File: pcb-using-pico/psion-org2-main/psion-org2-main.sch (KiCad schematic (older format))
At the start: 83 parts, among them J1 Conn_01x24_Female, J2 Conn_01x03_Female, J3 Conn_01x27_Female, J4 Conn_01x02_Female, J5 Conn_01x02_Female, J6 Conn_01x11_Female, M1 P-CHANNEL-MOSFET, M2 P-CHANNEL-MOSFET, M3 P-CHANNEL-MOSFET, U1 Pico, U10 AMS1117-3.3, U2 74HC595, U3 Regulator_Switching_MT3608, U4 74LS165, U5 74HC595, U6 AMS1117-5.0, U7 MCP7940N-xSN, Y1 32k768Hz

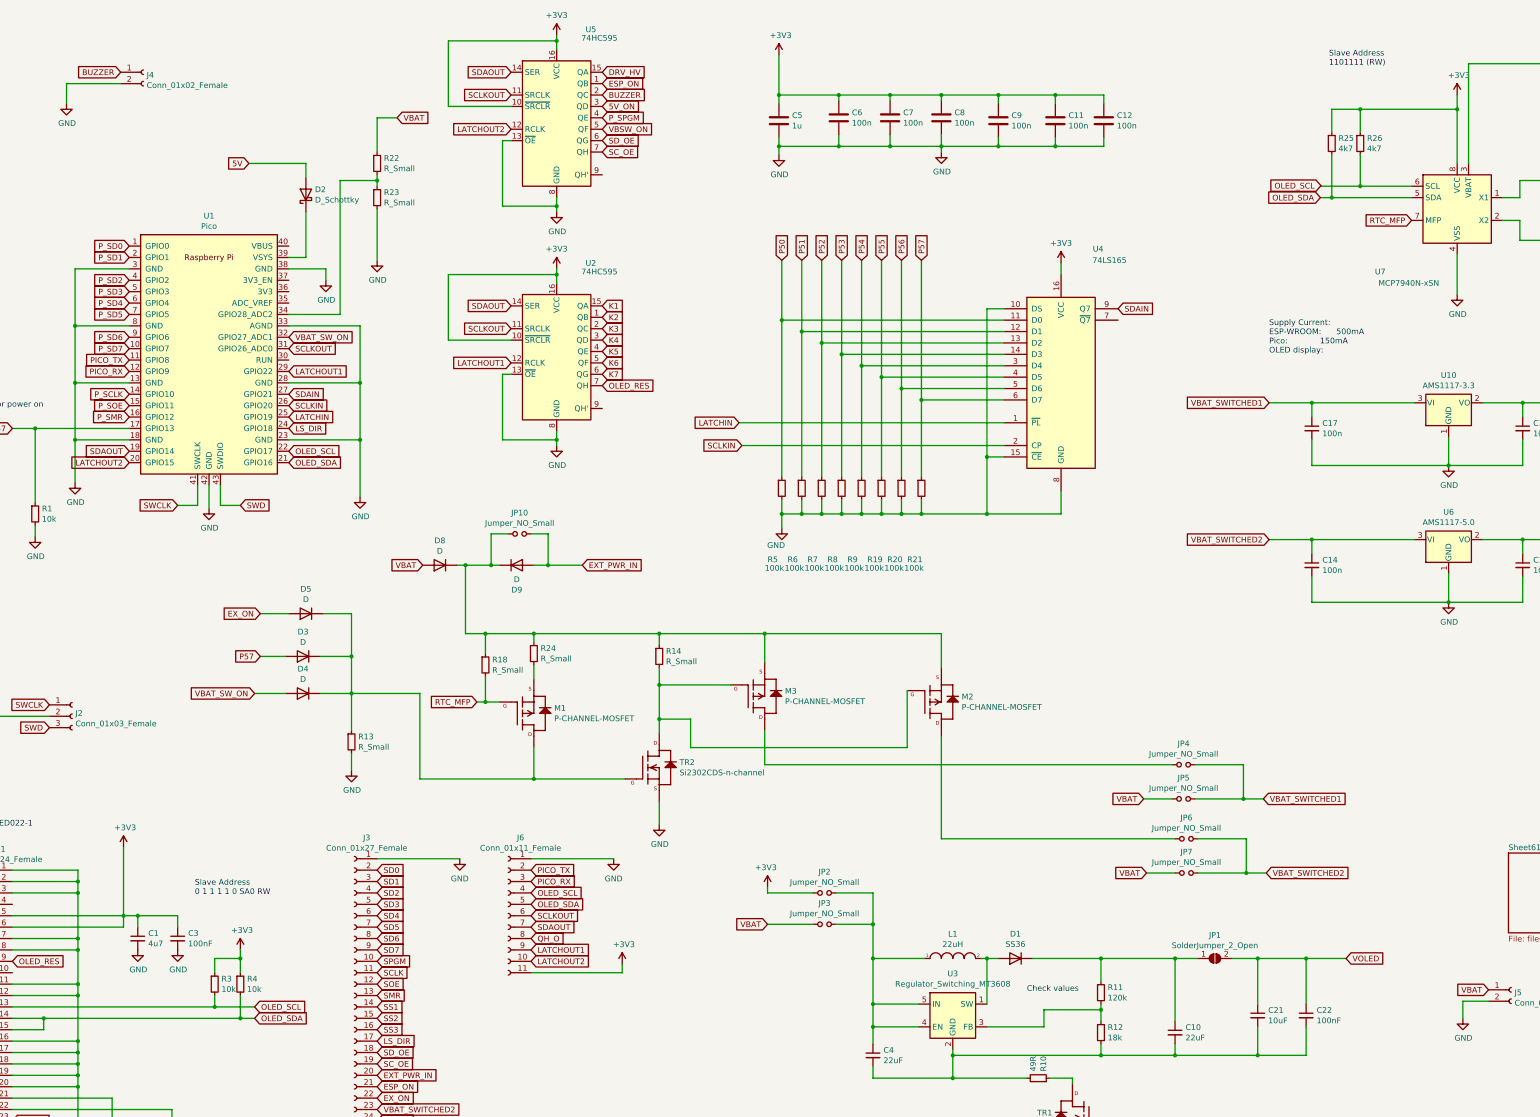
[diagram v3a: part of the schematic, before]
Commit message: First main PCB layout
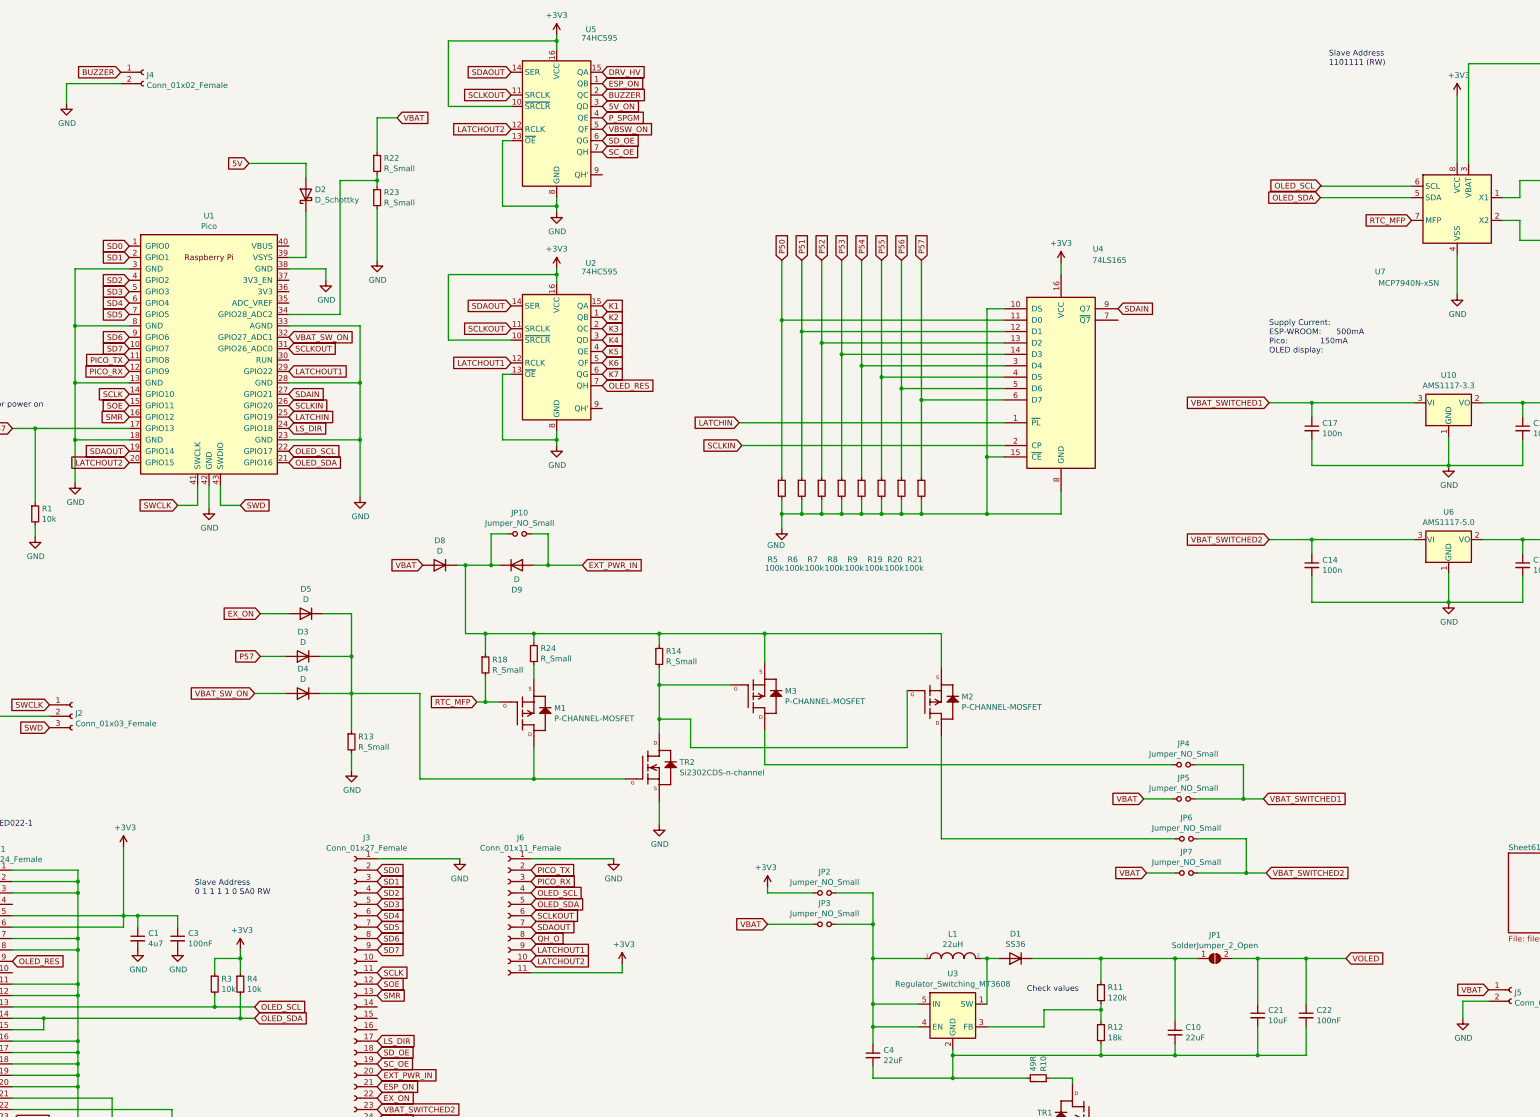
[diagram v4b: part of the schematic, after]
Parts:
- removed C11, C12, C6, C7, C8, C9: 100n, Capacitor_SMD:C_0805_2012Metric, symbol Device:C
- removed C5: 1u, Capacitor_SMD:C_0805_2012Metric, symbol Device:C
- removed R25, R26: 4k7, Resistor_SMD:R_0805_2012Metric, symbol Device:R_Small
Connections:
- net P_SCLK is gone; now on net SCLK: U1.14 (GPIO10)
- net P_SD0 is gone; now on net SD0: U1.1 (GPIO0)
- net P_SD1 is gone; now on net SD1: U1.2 (GPIO1)
- net P_SD2 is gone; now on net SD2: U1.4 (GPIO2)
- net P_SD3 is gone; now on net SD3: U1.5 (GPIO3)
- net P_SD4 is gone; now on net SD4: U1.6 (GPIO4)
- net P_SD5 is gone; now on net SD5: U1.7 (GPIO5)
- net P_SD6 is gone; now on net SD6: U1.9 (GPIO6)
- net P_SD7 is gone; now on net SD7: U1.10 (GPIO7)
- net P_SMR is gone; now on net SMR: U1.16 (GPIO12)
- net P_SOE is gone; now on net SOE: U1.15 (GPIO11)
- net SPGM: no longer names the net of J3.10 (Pin_10)
- net SS1: no longer names the net of J3.14 (Pin_14)
- net SS2: no longer names the net of J3.15 (Pin_15)
- net SS3: no longer names the net of J3.16 (Pin_16)

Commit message: Updates after fab1
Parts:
- D7: value 4v7 -> nopop
- R11: value 120k -> 110k
- R12: value 18k -> 4k7
- R27: value R_Small -> 110k
- R28: value R_Small -> 47k
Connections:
- net P_SPGM is gone; now on net SPGM: U5.4 (QE)
- net SPGM: now reaches J3.10 (Pin_10)
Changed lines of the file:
@@
 	2875 4775 2875 4975
 Text GLabel 6325 1550 2    50   Input ~ 0
-P_SPGM
+SPGM
 Text GLabel 2175 4575 0    50   Input ~ 0
 LATCHOUT2
@@
 AR Path="/61545310" Ref="R12"  Part="1"
 F 0 "R12" H 10759 9621 50  0000 L CNN
-F 1 "18k" H 10759 9530 50  0000 L CNN
+F 1 "4k7" H 10759 9530 50  0000 L CNN
 F 2 "Resistor_SMD:R_0805_2012Metric" H 10700 9575 50  0001 C CNN
 F 3 "~" H 10700 9575 50  0001 C CNN
@@
 AR Path="/6154534B" Ref="R11"  Part="1"
 F 0 "R11" H 10759 9271 50  0000 L CNN
-F 1 "120k" H 10759 9180 50  0000 L CNN
+F 1 "110k" H 10759 9180 50  0000 L CNN
 F 2 "Resistor_SMD:R_0805_2012Metric" H 10700 9225 50  0001 C CNN
 F 3 "~" H 10700 9225 50  0001 C CNN
@@
 AR Path="/61F7C995" Ref="R28"  Part="1"
 F 0 "R28" H 15084 1321 50  0000 L CNN
-F 1 "R_Small" H 15084 1230 50  0000 L CNN
+F 1 "47k" H 15084 1230 50  0000 L CNN
 F 2 "Resistor_SMD:R_0805_2012Metric" H 15025 1275 50  0001 C CNN
 F 3 "~" H 15025 1275 50  0001 C CNN
@@
 AR Path="/61F7C99B" Ref="R27"  Part="1"
 F 0 "R27" H 15084 896 50  0000 L CNN
-F 1 "R_Small" H 15084 805 50  0000 L CNN
+F 1 "110k" H 15084 805 50  0000 L CNN
 F 2 "Resistor_SMD:R_0805_2012Metric" H 15025 850 50  0001 C CNN
 F 3 "~" H 15025 850 50  0001 C CNN
@@
 AR Path="/61F7C9A1" Ref="D7"  Part="1"
 F 0 "D7" V 14604 1404 50  0000 L CNN
-F 1 "4v7" V 14695 1404 50  0000 L CNN
+F 1 "nopop" V 14695 1404 50  0000 L CNN
 F 2 "Diode_SMD:D_SOD-123" H 14650 1325 50  0001 C CNN
 F 3 "~" H 14650 1325 50  0001 C CNN
@@
 	1    0    0    -1
 $EndComp
+Text GLabel 4350 8950 2    50   Input ~ 0
+SPGM
 $EndSCHEMATC

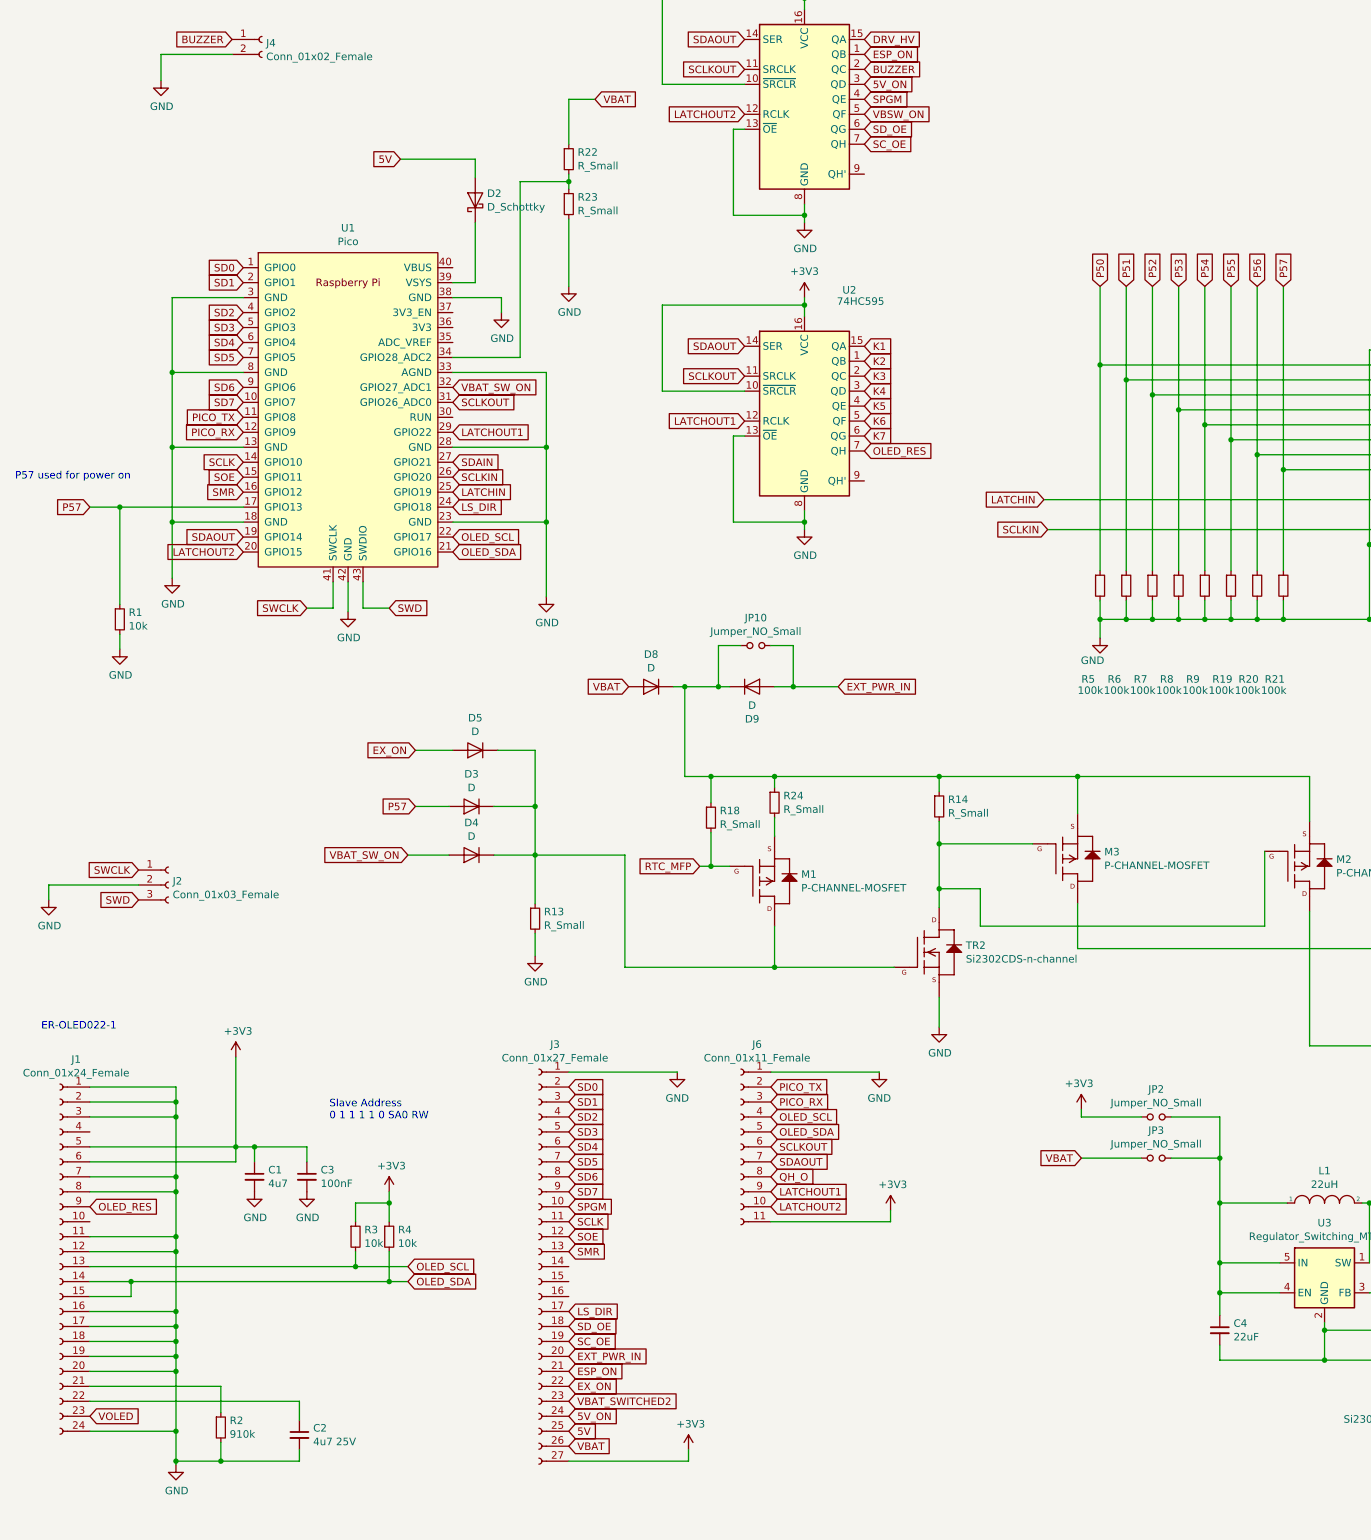
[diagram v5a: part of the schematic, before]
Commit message: Annotated ROM listin gupdate
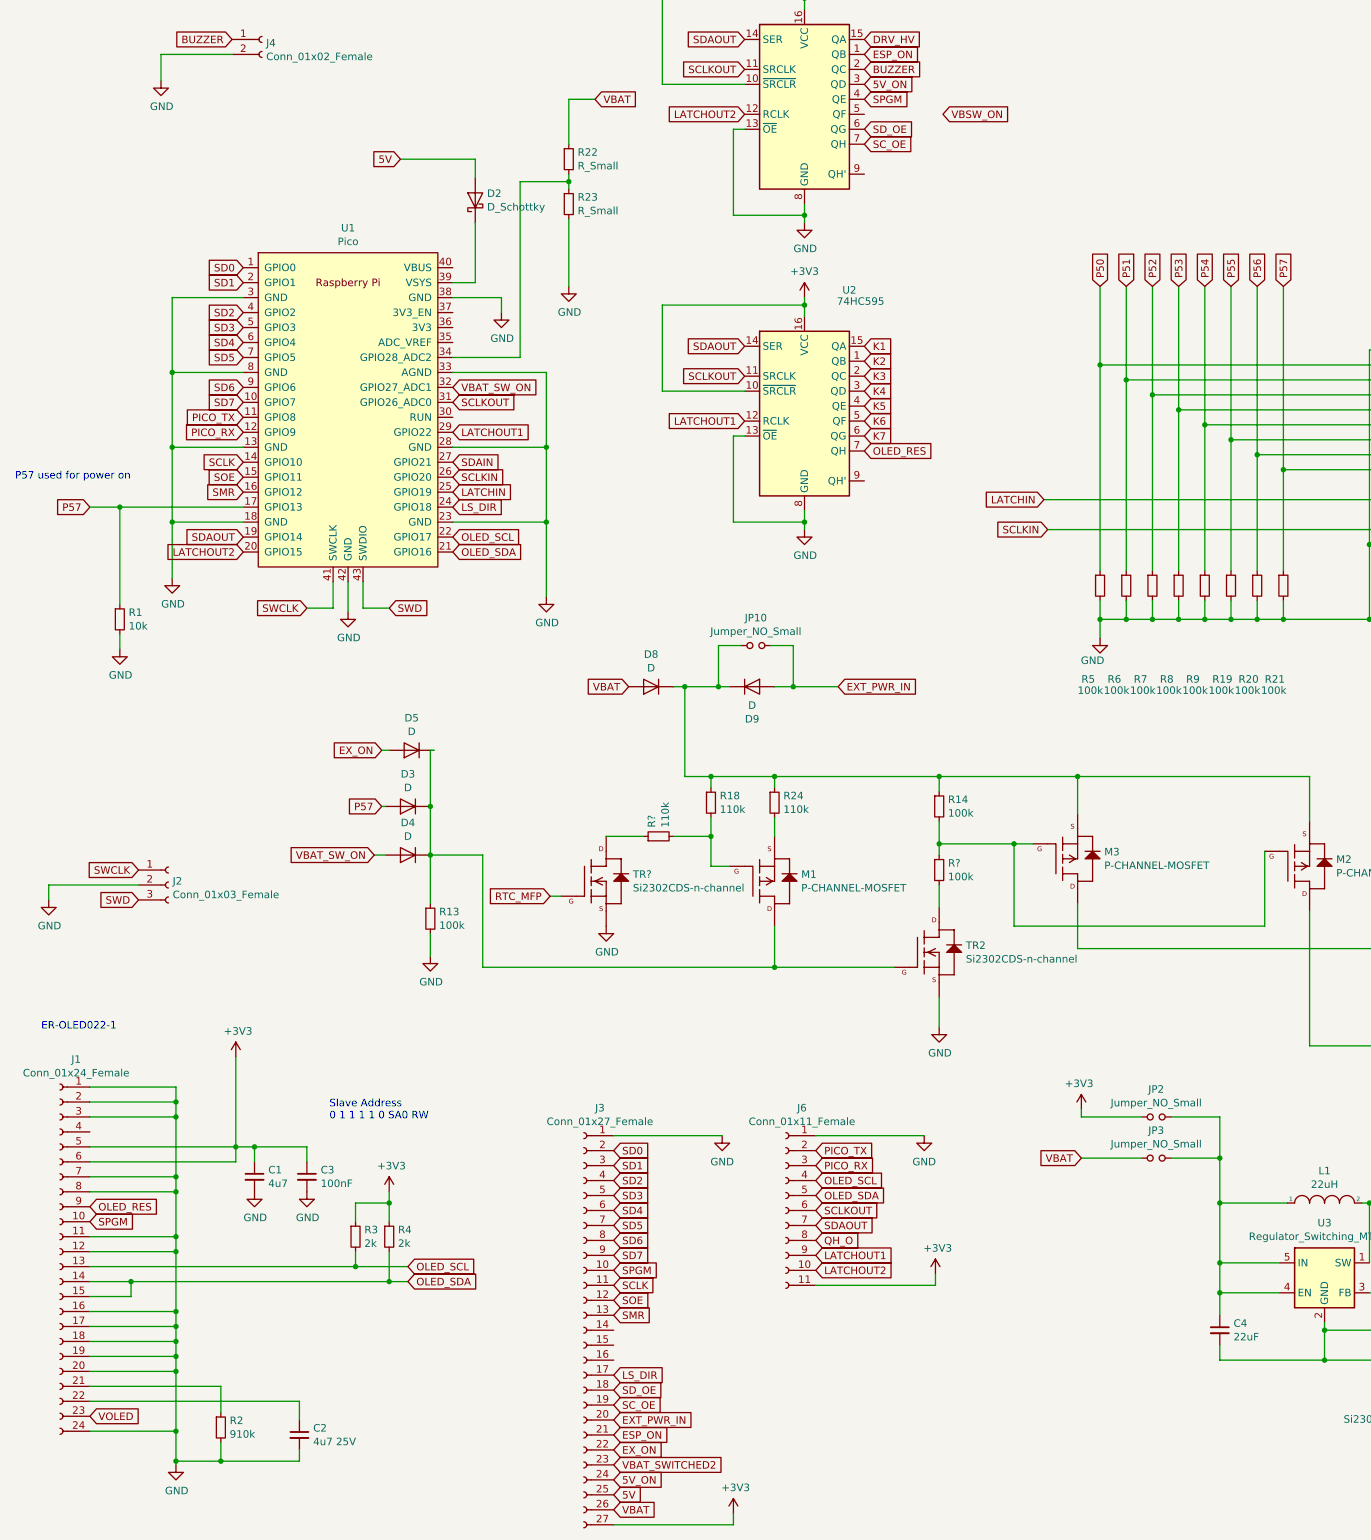
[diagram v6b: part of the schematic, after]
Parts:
- added R?: 100k, Resistor_SMD:R_0805_2012Metric, symbol Device:R_Small
- added R?: 110k, Resistor_SMD:R_0805_2012Metric, symbol Device:R_Small
- added TR?: Si2302CDS-n-channel, Package_TO_SOT_SMD:SOT-23, symbol New_Library:Si2302CDS-n-channel
- R13, R14: value R_Small -> 100k
- R18, R24: value R_Small -> 110k
- R3, R4: value 10k -> 2k
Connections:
- net GND: now also TR?.2 (S)
- net RTC_MFP: now also TR?.1 (G); no longer M1.1 (G), R18.2
- net SPGM: now also J1.10 (Pin_10)
- net VBSW_ON: no longer U5.5 (QF)
- net at M2.1 (G), M3.1 (G), R14.2: now also R?.1; no longer TR2.3 (D)
- new net: R?.2, TR2.3 (D)
- new net: M1.1 (G), R18.2, R?.2
- new net: R?.1, TR?.3 (D)
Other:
- moved on the sheet: D3, D4, D5, J3, J6, R13, R18

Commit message: V1.1 started
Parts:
- removed C14, C15: 100n, Capacitor_SMD:C_0805_2012Metric, symbol Device:C_Small
- removed JP10: Jumper_NO_Small, Jumper:SolderJumper-2_P1.3mm_Open_RoundedPad1.0x1.5mm, symbol Device:Jumper_NO_Small
- removed R10: 49R, Resistor_SMD:R_0805_2012Metric, symbol Device:R_Small
- removed R15: R_Small, Resistor_SMD:R_0805_2012Metric, symbol Device:R_Small
- removed TR1: Si2302CDS-n-channel, Package_TO_SOT_SMD:SOT-23, symbol New_Library:Si2302CDS-n-channel
- removed U6: AMS1117-5.0, Package_TO_SOT_SMD:SOT-223-3_TabPin2, symbol pak_breakout:AMS1117-5.0
- added C5, C6, C7: C_Small, Capacitor_SMD:C_0805_2012Metric, symbol Device:C_Small
- added D10, D11: 4v7, Diode_SMD:D_SOD-123, symbol Device:D_Zener
- added D12, D13, D14, D15, D16, D17, D18: 1N4148, Diode_SMD:D_SOD-123, symbol Device:D
- added R25: 10k, Resistor_SMD:R_0805_2012Metric, symbol Device:R_Small
- M1: value P-CHANNEL-MOSFET -> P-CH-MOSFET
- TR1: renamed from TR?; value Si2302CDS-n-channel -> Si2302CDS-n-ch
- gave numbers to parts that had none: 2
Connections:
- net +3V3: now also C5.1, C6.1, C7.1, R25.1
- net BUZZER: now also J3.14 (Pin_14)
- net GND: now also C10.2, C21.2, C22.2, C4.2, J1.10 (Pin_10), R12.2, U3.2 (GND), C5.2, C6.2, C7.2
- net K1: now also D12.1 (K); no longer U2.15 (QA)
- net K2: now also D13.1 (K); no longer U2.1 (QB)
- net K3: now also D14.1 (K); no longer U2.2 (QC)
- net K4: now also D15.1 (K); no longer U2.3 (QD)
- net K5: now also D16.1 (K); no longer U2.4 (QE)
- net K6: now also D17.1 (K); no longer U2.5 (QF)
- net K7: now also D18.1 (K); no longer U2.6 (QG)
- net QH_O: now also U5.9 (QH')
- net RTC_MFP: now also R25.2
- net SPGM: no longer J1.10 (Pin_10)
- net VBAT: now also D8.1 (K), D9.1 (K), M2.2 (S), M3.2 (S), R14.1, R18.1, R24.1, D10.1 (K), D11.1 (K); no longer D8.2 (A), J5.1 (Pin_1)
- net VBAT_SWITCHED1: now also J3.15 (Pin_15)
- net at M1.1 (G), R10.2, R18.2: now also D10.2 (A)
- net at M2.1 (G), M3.1 (G), R14.2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: now also D11.2 (A)
- new net: D13.2 (A), U2.1 (QB)
- new net: D12.2 (A), U2.15 (QA)
- new net: D14.2 (A), U2.2 (QC)
- new net: D15.2 (A), U2.3 (QD)
- new net: D16.2 (A), U2.4 (QE)
- new net: D17.2 (A), U2.5 (QF)
- new net: D18.2 (A), U2.6 (QG)
- new net BATCON: D8.2 (A), J5.1 (Pin_1)
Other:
- note added: "*NOTE*: Part is MCP7940N, \nthe 'M' suffix part has no VBAT pin."
